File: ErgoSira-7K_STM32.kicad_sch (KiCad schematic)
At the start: 25 parts, among them SW2 SW_Push, U1 XC6206PxxxMR, U2 STM32G431KBTx, U3 USBLC6-2SC6

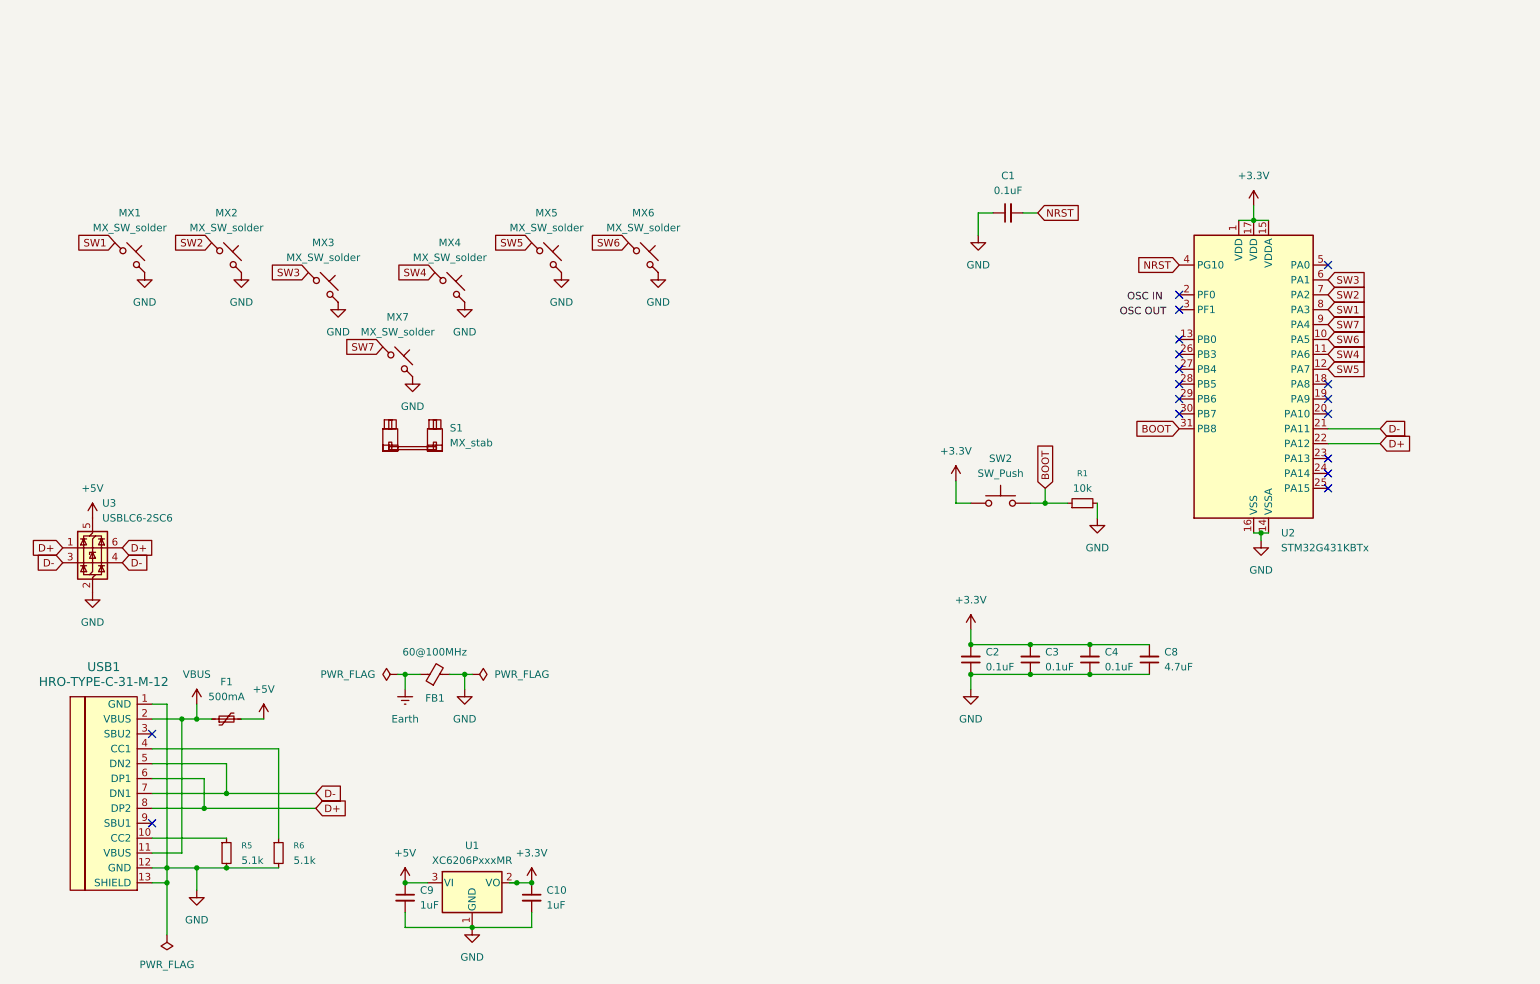
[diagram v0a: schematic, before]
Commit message: changed usb footprint 3d model
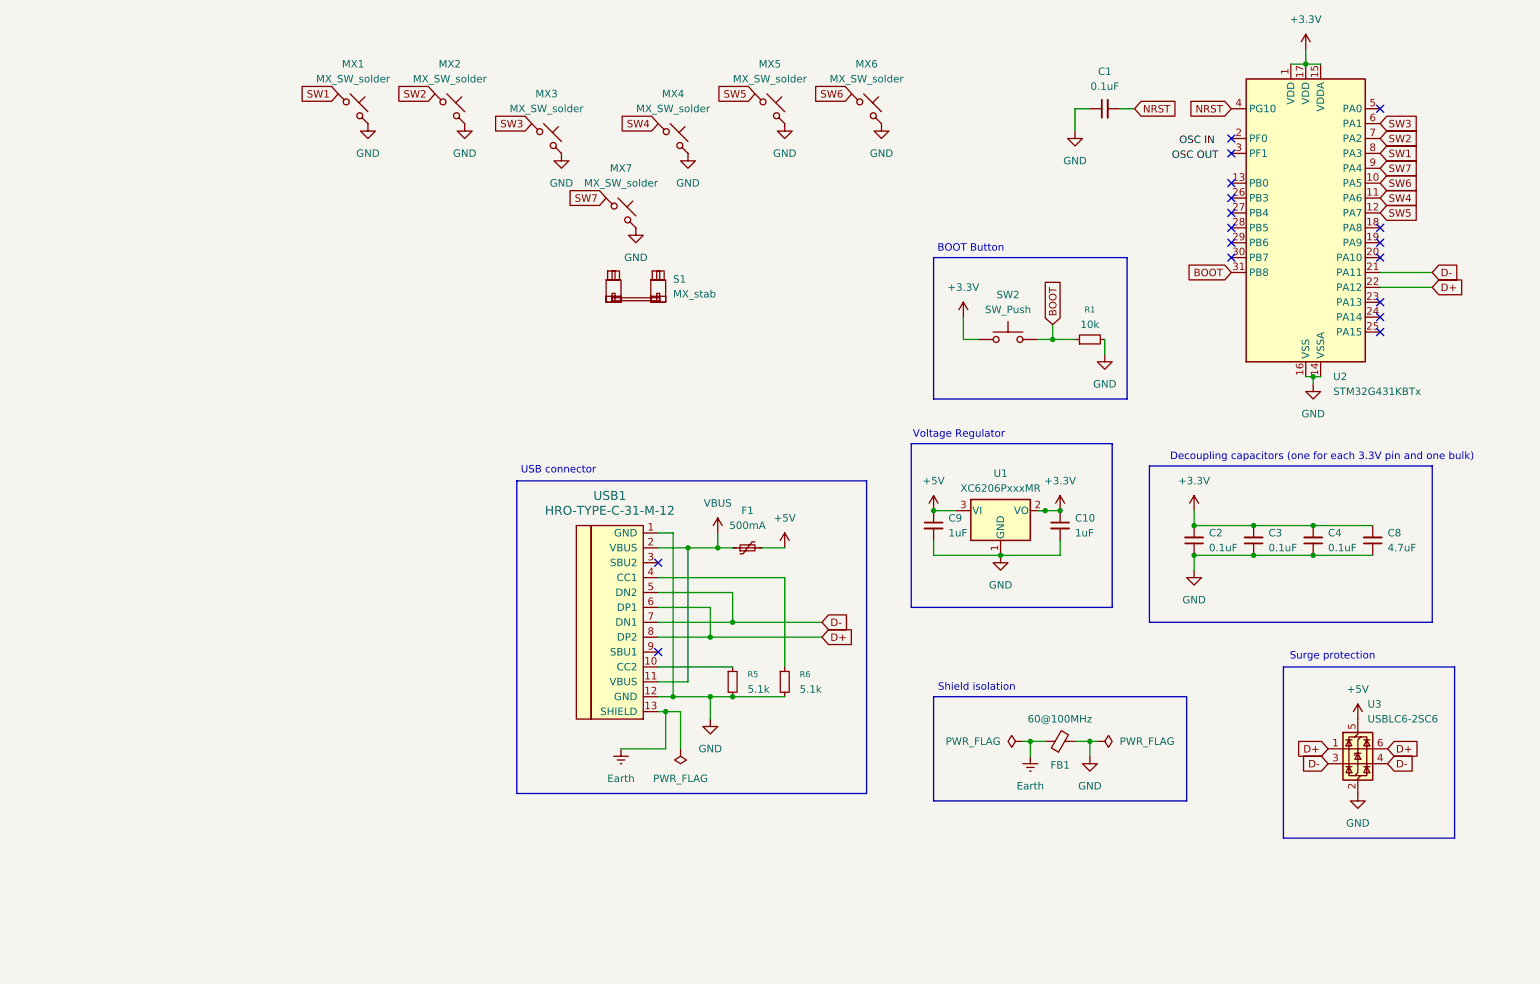
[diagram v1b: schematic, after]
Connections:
- net Earth: now also USB1.13 (SHIELD)
- net GND: no longer USB1.13 (SHIELD)
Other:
- note added: "BOOT Button"
- note added: "Decoupling capacitors (one for each 3.3V pin and one bulk)"
- note added: "Shield isolation"
- note added: "Surge protection"
- note added: "USB connector"
- note added: "Voltage Regulator"
- moved on the sheet: C1, C10, C2, C3, C4, C8, C9, F1, FB1, MX1, MX2, MX3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

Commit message: idk
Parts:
- removed S1: MX_stab, marbastlib-mx:STAB_MX_6.25u, symbol marbastlib-mx:MX_stab
- added MX8: MX_SW_solder, marbastlib-mx:SW_MX_1u, symbol marbastlib-mx:MX_SW_solder
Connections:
- net GND: now also MX8.2
- net SW1: now also U2.27 (PB4); no longer U2.8 (PA3)
- net SW2: now also U2.26 (PB3); no longer U2.7 (PA2)
- net SW3: now also U2.28 (PB5); no longer U2.6 (PA1)
- net SW7: now also U2.7 (PA2); no longer U2.9 (PA4)
- new net SW8: MX8.1, U2.8 (PA3)
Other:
- moved on the sheet: MX7
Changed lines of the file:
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@@
 	)
 	(no_connect
-		(at 237.49 50.8)
-	)
-	(no_connect
 		(at 262.89 53.34)
 	)
@@
 	)
 	(no_connect
+		(at 265.43 45.72)
+	)
+	(no_connect
 		(at 262.89 66.04)
 	)
@@
 	)
 	(no_connect
-		(at 237.49 53.34)
+		(at 237.49 55.88)
 	)
 	(no_connect
-		(at 237.49 48.26)
+		(at 262.89 58.42)
 	)
 	(no_connect
-		(at 237.49 55.88)
+		(at 262.89 35.56)
 	)
 	(no_connect
-		(at 262.89 58.42)
+		(at 262.89 71.12)
 	)
 	(no_connect
-		(at 262.89 71.12)
+		(at 262.89 43.18)
 	)
 	(wire
@@
 	(global_label "SW2"
 		(shape input)
-		(at 262.89 38.1 0)
+		(at 237.49 48.26 180)
 		(fields_autoplaced yes)
 		(effects
@@
 				(size 1.27 1.27)
 			)
-			(justify left)
+			(justify right)
 		)
 		(property "Intersheetrefs" "${INTERSHEET_REFS}"
-			(at 269.7456 38.1 0)
+			(at 230.6344 48.26 0)
 			(effects
 				(font
 					(size 1.27 1.27)
 				)
-				(justify left)
+				(justify right)
 				(hide yes)
 			)
@@
 	(global_label "SW1"
 		(shape input)
-		(at 262.89 40.64 0)
+		(at 237.49 50.8 180)
 		(fields_autoplaced yes)
 		(effects
@@
 				(size 1.27 1.27)
 			)
-			(justify left)
+			(justify right)
 		)
 		(property "Intersheetrefs" "${INTERSHEET_REFS}"
-			(at 269.7456 40.64 0)
+			(at 230.6344 50.8 0)
 			(effects
 				(font
 					(size 1.27 1.27)
 				)
-				(justify left)
+				(justify right)
 				(hide yes)
 			)
@@
 		)
 	)
+	(global_label "SW8"
+		(shape input)
+		(at 262.89 40.64 0)
+		(fields_autoplaced yes)
+		(effects
+			(font
+				(size 1.27 1.27)
+			)
+			(justify left)
+		)
+		(property "Intersheetrefs" "${INTERSHEET_REFS}"
+			(at 269.7456 40.64 0)
+			(effects
+				(font
+					(size 1.27 1.27)
+				)
+				(justify left)
+				(hide yes)
+			)
+		)
+	)
 	(global_label "D+"
 		(shape input)
@@
 	(global_label "SW7"
 		(shape input)
-		(at 130.81 48.26 180)
+		(at 118.11 54.61 180)
 		(fields_autoplaced yes)
 		(effects
@@
 		)
 		(property "Intersheetrefs" "${INTERSHEET_REFS}"
-			(at 123.9544 48.26 0)
+			(at 111.2544 54.61 0)
 			(effects
 				(font
@@
 		)
 	)
+	(global_label "SW8"
+		(shape input)
+		(at 139.7 54.61 180)
+		(fields_autoplaced yes)
+		(effects
+			(font
+				(size 1.27 1.27)
+			)
+			(justify right)
+		)
+		(property "Intersheetrefs" "${INTERSHEET_REFS}"
+			(at 132.8444 54.61 0)
+			(effects
+				(font
+					(size 1.27 1.27)
+				)
+				(justify right)
+				(hide yes)
+			)
+		)
+	)
 	(global_label "SW7"
 		(shape input)
-		(at 262.89 43.18 0)
+		(at 262.89 38.1 0)
 		(fields_autoplaced yes)
 		(effects
@@
 		)
 		(property "Intersheetrefs" "${INTERSHEET_REFS}"
-			(at 269.7456 43.18 0)
+			(at 269.7456 38.1 0)
 			(effects
 				(font
@@
 	(global_label "SW3"
 		(shape input)
-		(at 262.89 35.56 0)
+		(at 237.49 53.34 180)
 		(fields_autoplaced yes)
 		(effects
@@
 				(size 1.27 1.27)
 			)
-			(justify left)
+			(justify right)
 		)
 		(property "Intersheetrefs" "${INTERSHEET_REFS}"
-			(at 269.7456 35.56 0)
+			(at 230.6344 53.34 0)
 			(effects
 				(font
 					(size 1.27 1.27)
 				)
-				(justify left)
+				(justify right)
 				(hide yes)
 			)
@@
 	)
 	(symbol
-		(lib_id "marbastlib-mx:MX_stab")
-		(at 135.89 63.5 0)
-		(unit 1)
-		(exclude_from_sim no)
-		(in_bom yes)
-		(on_board yes)
-		(dnp no)
-		(fields_autoplaced yes)
-		(property "Reference" "S1"
-			(at 142.24 62.1029 0)
-			(effects
-				(font
-					(size 1.27 1.27)
-				)
-				(justify left)
-			)
-		)
-		(property "Value" "MX_stab"
-			(at 142.24 64.6429 0)
-			(effects
-				(font
-					(size 1.27 1.27)
-				)
-				(justify left)
-			)
-		)
-		(property "Footprint" "marbastlib-mx:STAB_MX_6.25u"
-			(at 135.89 63.5 0)
-			(effects
-				(font
-					(size 1.27 1.27)
-				)
-				(hide yes)
-			)
-		)
-		(property "Datasheet" ""
-			(at 135.89 63.5 0)
-			(effects
-				(font
-					(size 1.27 1.27)
-				)
-				(hide yes)
-			)
-		)
-		(property "Description" "Cherry MX-style stabilizer"
-			(at 135.89 63.5 0)
-			(effects
-				(font
-					(size 1.27 1.27)
-				)
-				(hide yes)
-			)
-		)
-		(instances
-			(project ""
-				(path "/a8954c97-0c11-4840-a90b-f04daf5a572b"
-					(reference "S1")
-					(unit 1)
-				)
-			)
-		)
-	)
-	(symbol
 		(lib_id "Device:R_Small")
 		(at 161.29 130.81 0)
@@
 	(symbol
 		(lib_id "marbastlib-mx:MX_SW_solder")
-		(at 133.35 50.8 0)
+		(at 120.65 57.15 0)
 		(unit 1)
 		(exclude_from_sim no)
@@
 		(fields_autoplaced yes)
 		(property "Reference" "MX7"
-			(at 133.35 43.18 0)
+			(at 120.65 49.53 0)
 			(effects
 				(font
@@
 		)
 		(property "Value" "MX_SW_solder"
-			(at 133.35 45.72 0)
+			(at 120.65 52.07 0)
 			(effects
 				(font
@@
 		)
 		(property "Footprint" "marbastlib-mx:SW_MX_1u"
-			(at 133.35 50.8 0)
+			(at 120.65 57.15 0)
 			(effects
 				(font
@@
 		)
 		(property "Datasheet" "~"
-			(at 133.35 50.8 0)
+			(at 120.65 57.15 0)
 			(effects
 				(font
@@
 		)
 		(property "Description" "Push button switch, normally open, two pins, 45° tilted"
-			(at 133.35 50.8 0)
+			(at 120.65 57.15 0)
 			(effects
 				(font
@@
 	(symbol
 		(lib_id "power:GND")
-		(at 135.89 53.34 0)
+		(at 123.19 59.69 0)
 		(unit 1)
 		(exclude_from_sim no)
@@
 		(fields_autoplaced yes)
 		(property "Reference" "#PWR018"
-			(at 135.89 59.69 0)
+			(at 123.19 66.04 0)
 			(effects
 				(font
@@
 		)
 		(property "Value" "GND"
-			(at 135.89 58.42 0)
+			(at 123.19 64.77 0)
 			(effects
 				(font
@@
 		)
 		(property "Footprint" ""
-			(at 135.89 53.34 0)
+			(at 123.19 59.69 0)
 			(effects
 				(font
@@
 		)
 		(property "Datasheet" ""
-			(at 135.89 53.34 0)
+			(at 123.19 59.69 0)
 			(effects
 				(font
@@
 		)
 		(property "Description" "Power symbol creates a global label with name \"GND\" , ground"
-			(at 135.89 53.34 0)
+			(at 123.19 59.69 0)
 			(effects
 				(font
@@
 	)
 	(symbol
+		(lib_id "power:GND")
+		(at 144.78 59.69 0)
+		(unit 1)
+		(exclude_from_sim no)
+		(in_bom yes)
+		(on_board yes)
+		(dnp no)
+		(fields_autoplaced yes)
+		(property "Reference" "#PWR026"
+			(at 144.78 66.04 0)
+			(effects
+				(font
+					(size 1.27 1.27)
+				)
+				(hide yes)
+			)
+		)
+		(property "Value" "GND"
+			(at 144.78 64.77 0)
+			(effects
+				(font
+					(size 1.27 1.27)
+				)
+			)
+		)
+		(property "Footprint" ""
+			(at 144.78 59.69 0)
+			(effects
+				(font
+					(size 1.27 1.27)
+				)
+				(hide yes)
+			)
+		)
+		(property "Datasheet" ""
+			(at 144.78 59.69 0)
+			(effects
+				(font
+					(size 1.27 1.27)
+				)
+				(hide yes)
+			)
+		)
+		(property "Description" "Power symbol creates a global label with name \"GND\" , ground"
+			(at 144.78 59.69 0)
+			(effects
+				(font
+					(size 1.27 1.27)
+				)
+				(hide yes)
+			)
+		)
+		(pin "1"
+		)
+		(instances
+			(project "ErgoSira-7K_STM32"
+				(path "/a8954c97-0c11-4840-a90b-f04daf5a572b"
+					(reference "#PWR026")
+					(unit 1)
+				)
+			)
+		)
+	)
+	(symbol
 		(lib_id "power:+3.3V")
 		(at 250.19 22.86 0)
@@
 					(unit 1)
 				)
+			)
+		)
+	)
+	(symbol
+		(lib_id "marbastlib-mx:MX_SW_solder")
+		(at 142.24 57.15 0)
+		(unit 1)
+		(exclude_from_sim no)
+		(in_bom yes)
+		(on_board yes)
+		(dnp no)
+		(fields_autoplaced yes)
+		(property "Reference" "MX8"
+			(at 142.24 49.53 0)
+			(effects
+				(font
+					(size 1.27 1.27)
+				)
+			)
+		)
+		(property "Value" "MX_SW_solder"
+			(at 142.24 52.07 0)
+			(effects
+				(font
+					(size 1.27 1.27)
+				)
+			)
+		)
+		(property "Footprint" "marbastlib-mx:SW_MX_1u"
+			(at 142.24 57.15 0)
+			(effects
+				(font
+					(size 1.27 1.27)
+				)
+				(hide yes)
+			)
+		)
+		(property "Datasheet" "~"
+			(at 142.24 57.15 0)
+			(effects
+				(font
+					(size 1.27 1.27)
+				)
+				(hide yes)
+			)
+		)
+		(property "Description" "Push button switch, normally open, two pins, 45° tilted"
+			(at 142.24 57.15 0)
+			(effects
+				(font
+					(size 1.27 1.27)
+				)
+				(hide yes)
+			)
+		)
+		(pin "2"
+		)
+		(pin "1"
+		)
+		(instances
+			(project "ErgoSira-7K_STM32"
+				(path "/a8954c97-0c11-4840-a90b-f04daf5a572b"
+					(reference "MX8")
+					(unit 1)
+				)
